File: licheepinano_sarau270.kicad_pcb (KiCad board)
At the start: 4 copper layers, 81.3 x 51.9 mm, 120 parts, among them Con1 SIM8050-6-0-14-01-A, Con2 >VALUE, Con3 USB_C_Wurth_632723130112, P1 RF2-03E-T-00-50-G, Q1 BC847B, Q2 BC847B, T1 FDN304P, U1 LAN9514I, U3 LILY-W132, U4 MAX-M8C, U5 TXB0104, U6 AP2127K-2.8TRG1, U7 LM317DCYR, X1 ABM3-25.000MHZ-D2Y-T

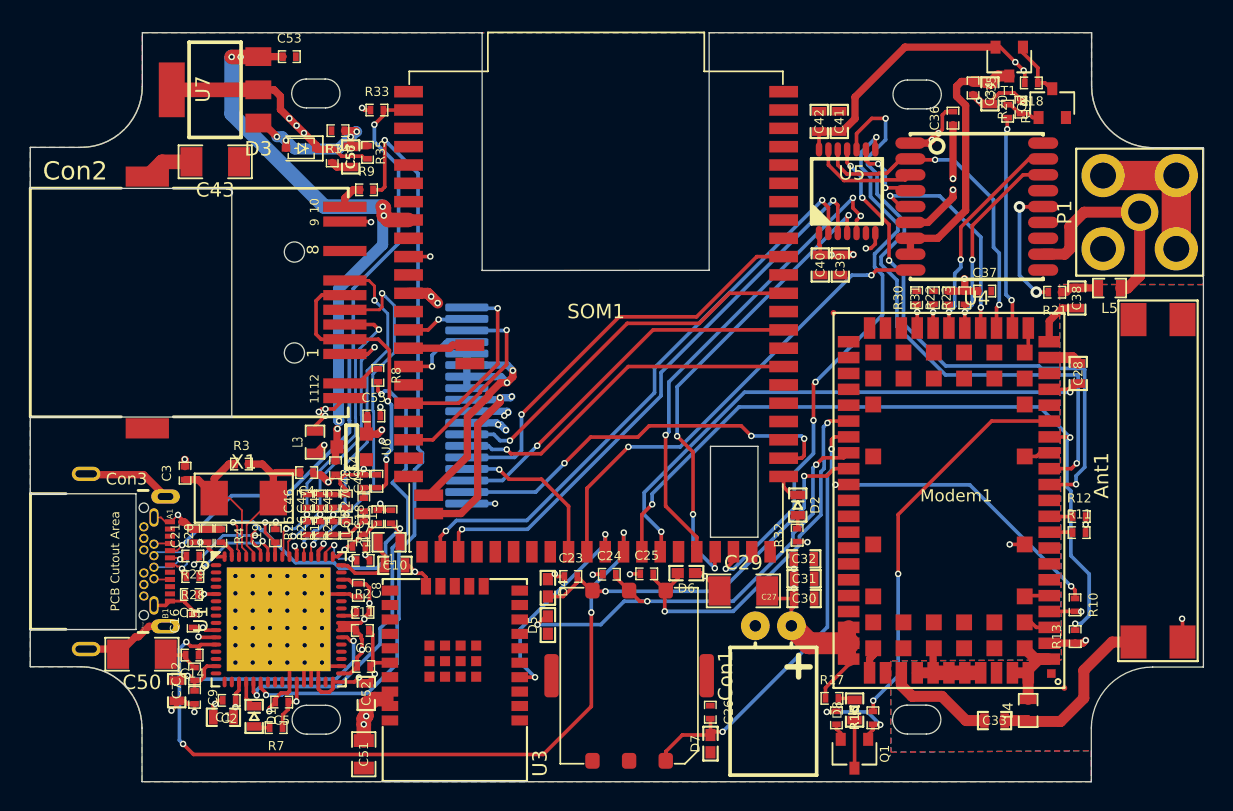
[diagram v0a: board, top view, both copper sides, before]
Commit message: Added all connections, usb and ethernet track not aligned yet, component references not aligned, gerbers not generated
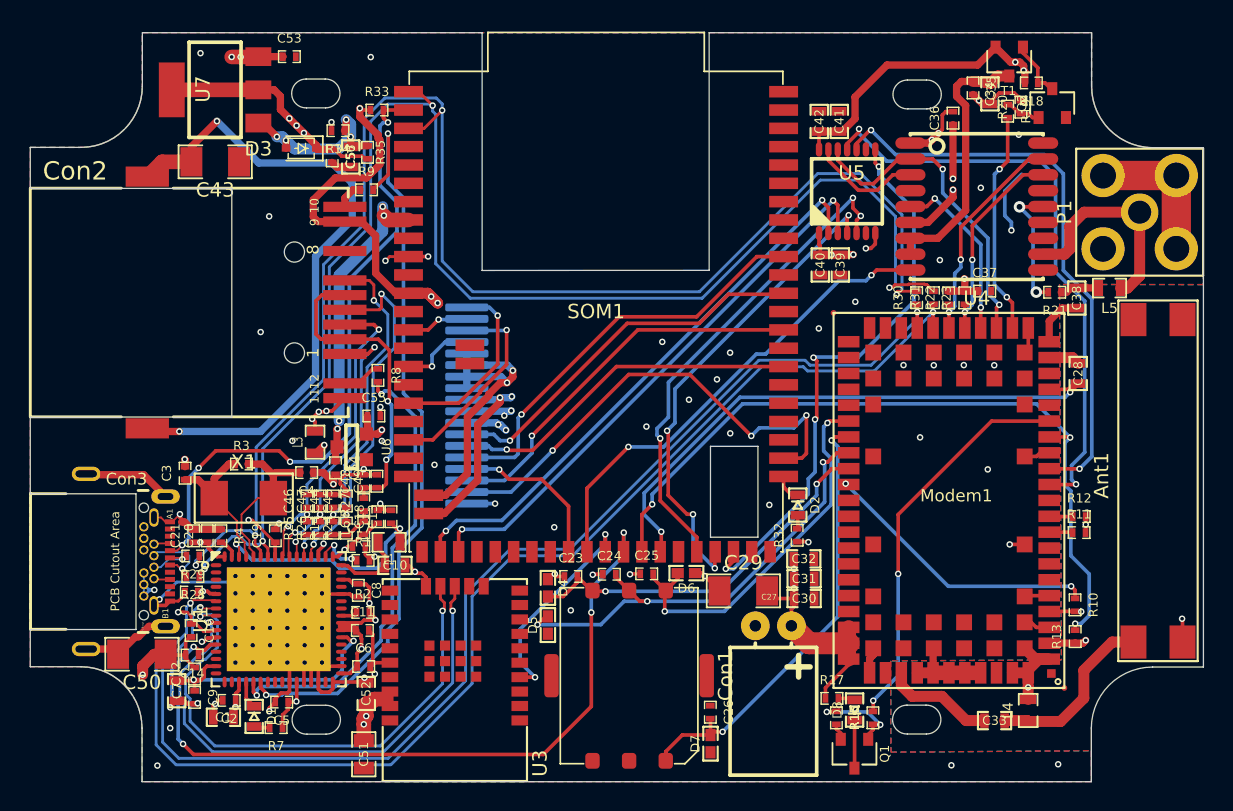
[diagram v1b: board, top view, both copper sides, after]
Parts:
- Con2: value >VALUE -> WE-RJ45_7498011122AR
- moved C16 0.66 mm to (110.4, 113.9), turned to 270 degrees
- moved C15 0.17 mm to (110.4, 111.2)
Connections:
- Con3 pad B2: (no net) -> /LicheePi Nano SOM/USB_ID
- Con3 pad B3: (no net) -> /LicheePi Nano SOM/USB_ID
- Modem1 pad 28: /USB Hub Module/USB_D2_OUT_N -> /USB Hub Module/USB_D4_OUT_N
- Modem1 pad 29: /USB Hub Module/USB_D2_OUT_P -> /USB Hub Module/USB_D4_OUT_P
- R30 pad 1: /USB Hub Module/USB_D2_OUT_P -> /USB Hub Module/USB_D4_OUT_P
- R31 pad 1: /USB Hub Module/USB_D2_OUT_N -> /USB Hub Module/USB_D4_OUT_N
- U1 pad 1: /USB Hub Module/USB_D2_OUT_N -> (no net)
- U1 pad 2: /USB Hub Module/USB_D2_OUT_P -> (no net)
- U1 pad 3: /USB Hub Module/USB_D3_OUT_N -> (no net)
- U1 pad 4: /USB Hub Module/USB_D3_OUT_P -> (no net)
- U1 pad 6: (no net) -> /USB Hub Module/USB_D4_OUT_N
- U1 pad 7: (no net) -> /USB Hub Module/USB_D4_OUT_P
- U1 pad 8: (no net) -> /USB Hub Module/USB_D5_OUT_N
- U1 pad 9: (no net) -> /USB Hub Module/USB_D5_OUT_P
- U3 pad 23: /USB Hub Module/USB_D3_OUT_P -> /USB Hub Module/USB_D5_OUT_P
- U3 pad 24: /USB Hub Module/USB_D3_OUT_N -> /USB Hub Module/USB_D5_OUT_N
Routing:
- net /LicheePi Nano SOM/USB_D_N: track 6.83 -> 103.4 mm, vias 2 -> 4
- net /LicheePi Nano SOM/USB_D_P: track 7.90 -> 104.3 mm, vias 2 -> 4
- net /USB Hub Module/USB_D4_OUT_N: track 0.00 -> 85.6 mm, vias 0 -> 2
- net /USB Hub Module/USB_D4_OUT_P: track 0.00 -> 83.2 mm, vias 0 -> 2
- net /Ethernet Connector Module/SHIELD1: track 3.48 -> 46.0 mm, vias 0 -> 2
- net /USB Hub Module/USB_D5_OUT_N: track 0.00 -> 37.5 mm, vias 0 -> 2
- net /USB Hub Module/USB_D5_OUT_P: track 0.00 -> 37.0 mm, vias 0 -> 2
- net GND: track 203.3 -> 235.4 mm, vias 30 -> 66
- net 3V3: track 53.4 -> 74.4 mm, vias 18 -> 17
- net /LicheePi Nano SOM/USB_ID: track 42.3 -> 52.9 mm, vias 2 -> 5
- net (no net): track 9.73 -> 0.00 mm, vias 2 -> 0
- net Net-(C50-Pad1): track 12.6 -> 21.9 mm
- net /LicheePi Nano SOM/GPIO_PD19: track 28.3 -> 33.6 mm
- net /Ethernet Connector Module/POWER_IN_3V3: track 43.4 -> 48.3 mm
- net /LicheePi Nano SOM/POWER_IN_5V0: track 70.8 -> 66.0 mm
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
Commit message: Aligned all sillks and generated BOM, Gerbser, Schematic PDF
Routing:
- net GND: track 235.4 -> 260.6 mm, vias 66 -> 78
- net Net-(C33-Pad2): track 7.65 -> 9.28 mm
- net /Modem 3G/MODEM_POWER_IN: track 92.0 -> 93.5 mm
- net Net-(Ant1-Pad1): track 12.4 -> 11.4 mm

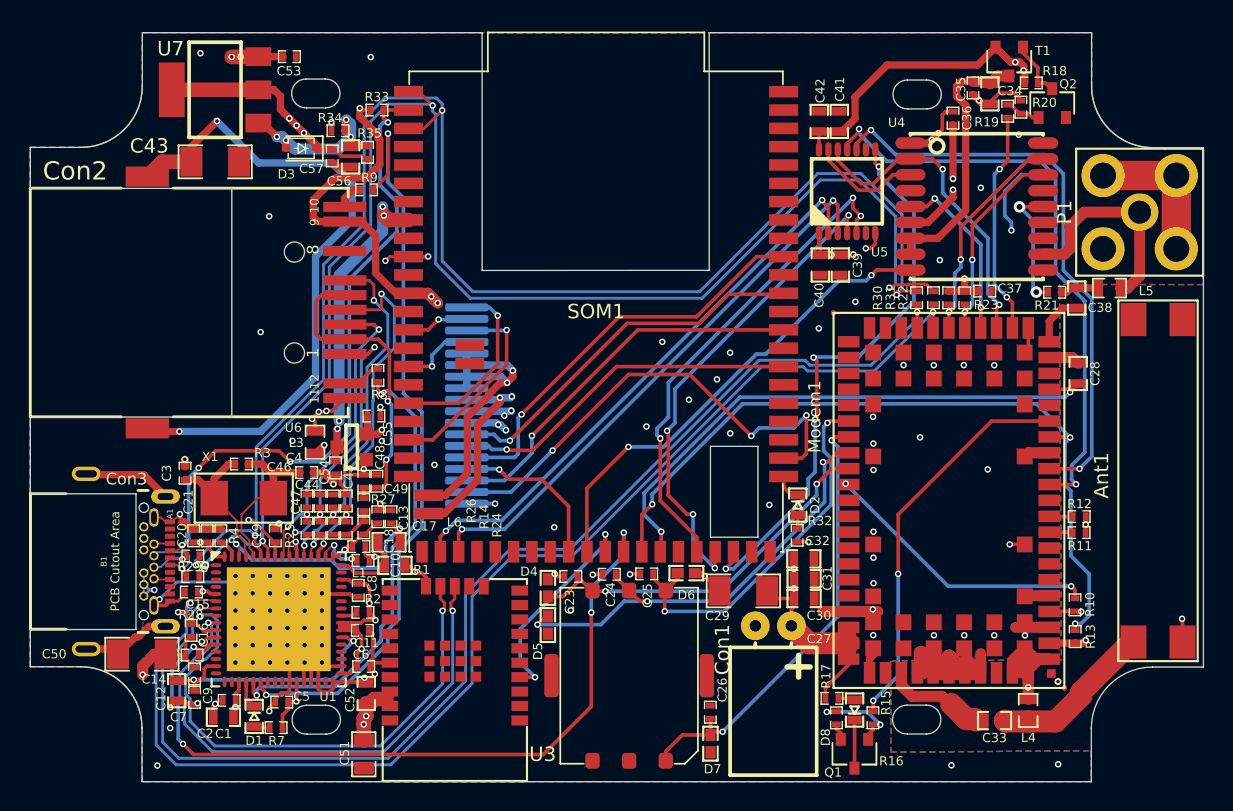
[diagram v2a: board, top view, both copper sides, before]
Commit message: Tuned high speed tracks
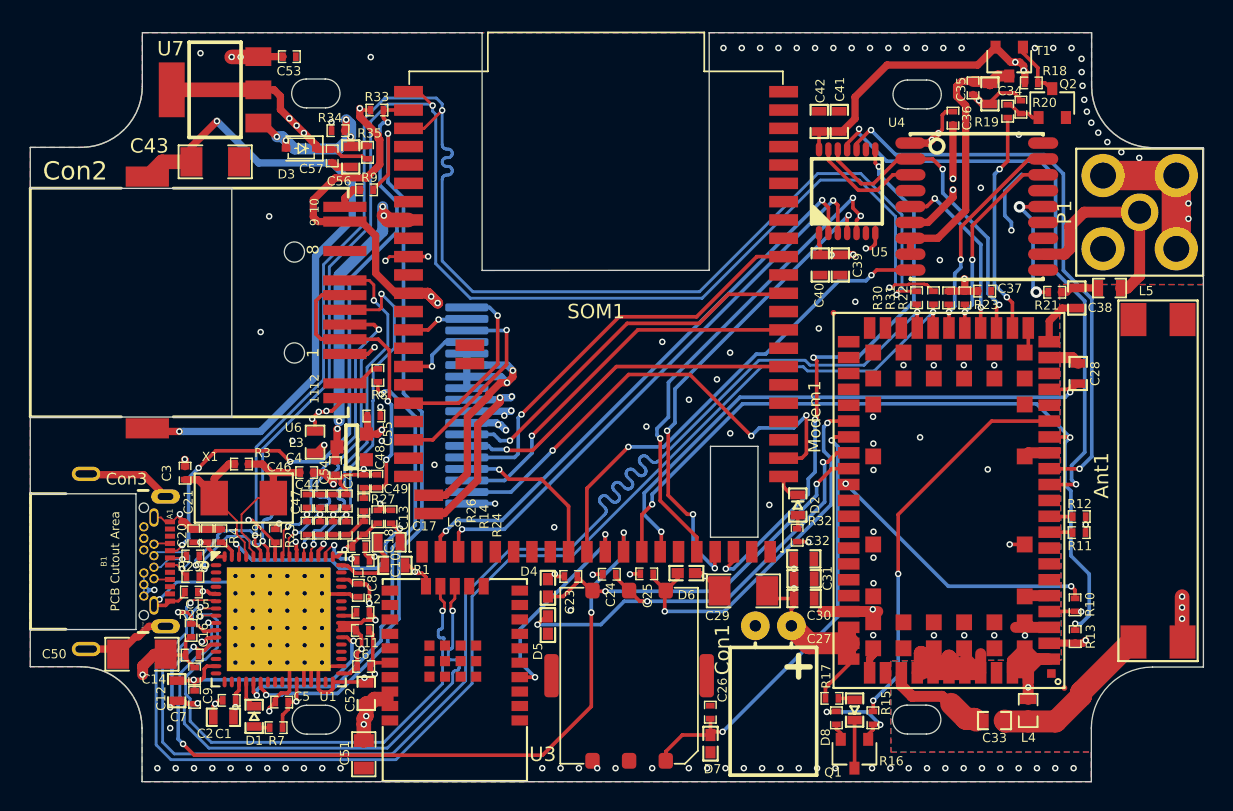
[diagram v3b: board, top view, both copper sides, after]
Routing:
- net GND: track 260.6 -> 268.3 mm, vias 78 -> 144
- net /USB Hub Module/USB_D4_OUT_P: track 83.2 -> 88.8 mm
- net /LicheePi Nano SOM/USB_D_P: track 104.3 -> 106.3 mm
- net /USB Hub Module/ETHERNET_TXP: track 20.5 -> 22.5 mm
- net /LicheePi Nano SOM/USB_D_N: track 103.4 -> 105.2 mm
- net /USB Hub Module/USB_D5_OUT_P: track 37.0 -> 37.8 mm
- net /USB Hub Module/ETHERNET_RXN: track 24.9 -> 25.6 mm

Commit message: Rotate sim card holder
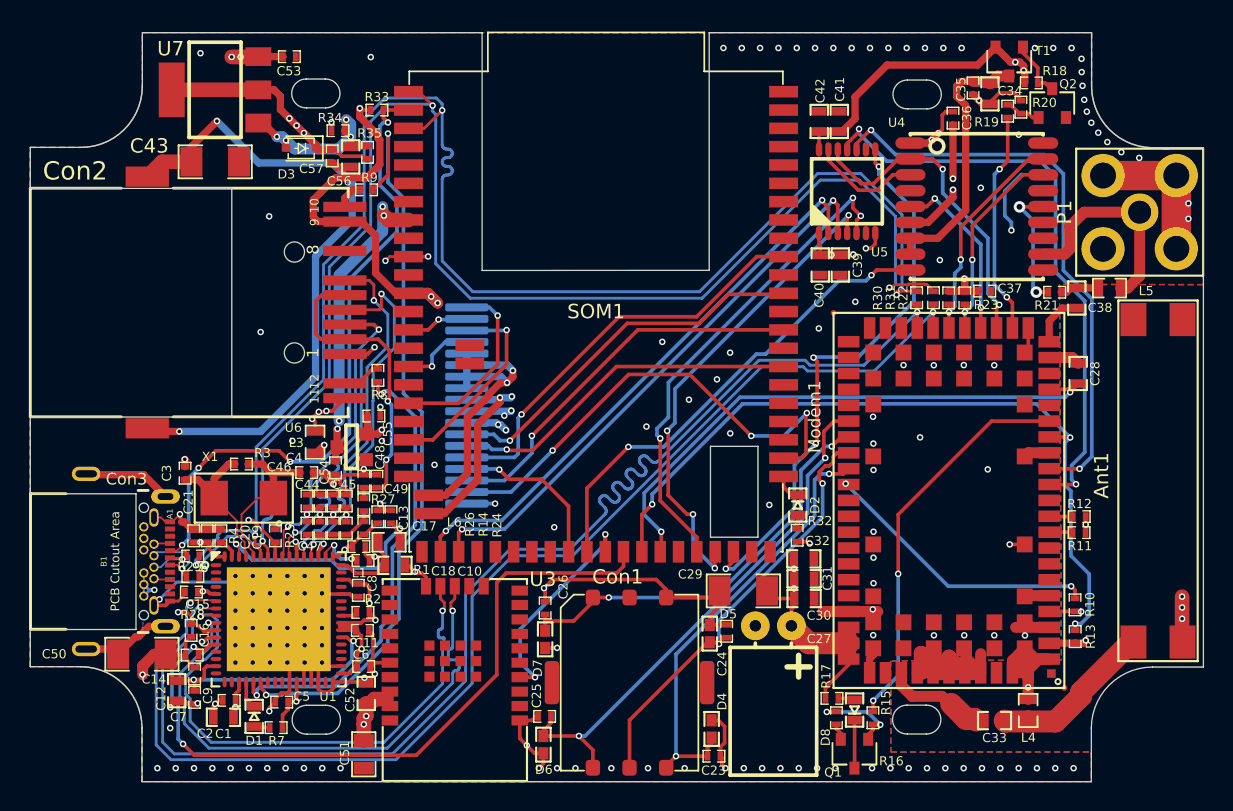
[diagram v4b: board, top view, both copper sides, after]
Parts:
- moved C23 15.9 mm to (146.6, 122.6), turned to 180 degrees
- moved D6 15.5 mm to (134.8, 121.8), turned to 270 degrees
- moved D4 15.0 mm to (146.5, 120.7)
- moved D7 13.6 mm to (134.9, 114.5)
- moved C26 13.5 mm to (134.9, 112.3)
- moved C25 12.2 mm to (134.9, 119.8)
- moved D5 11.2 mm to (146.3, 114.1), turned to 90 degrees
- moved C24 9.04 mm to (147.5, 113.9), turned to 270 degrees
- moved Con1 0.48 mm to (140.8, 117.5), turned to 90 degrees
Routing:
- net GND: track 268.3 -> 292.5 mm, vias 144 -> 140
- net /Modem 3G/SIM_CLK: track 26.7 -> 37.1 mm
- net /Modem 3G/VSIM: track 26.1 -> 30.5 mm
- net /LicheePi Nano SOM/GPIO_PD11: track 54.2 -> 50.9 mm, vias 4 -> 2
- net /Modem 3G/SIM_RST: track 32.5 -> 30.2 mm, vias 3 -> 2
- net /Modem 3G/SIM_IO: track 31.2 -> 29.3 mm

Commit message: Applied all issues
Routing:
- net /Logic Voltage Shifter/SIG4_HIGH_PART: track 34.1 -> 40.5 mm, vias 3 -> 5
- net /LicheePi Nano SOM/GPIO_PD0: track 53.1 -> 55.7 mm
- net /Logic Voltage Shifter/SIG3_HIGH_PART: track 33.7 -> 35.7 mm
- net /LicheePi Nano SOM/GPIO_PD1: track 40.0 -> 41.6 mm
- net /LicheePi Nano SOM/GPIO_PD9: track 33.1 -> 34.3 mm
- net /Logic Voltage Shifter/SIG2_HIGH_PART: track 39.2 -> 40.4 mm
- net /LCD Module/CS: track 29.2 -> 30.3 mm
- net /Modem 3G/MODEM_POWER_IN: track 93.5 -> 94.1 mm
- net /GPS Module/GPS_EXTINT: track 12.2 -> 12.8 mm
- net 3V3: track 74.5 -> 75.1 mm
- net GND: vias 140 -> 147
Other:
- outline, holes or cut-outs redrawn
